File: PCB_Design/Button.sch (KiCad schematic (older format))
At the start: 4 parts, among them SW1 SW_Push

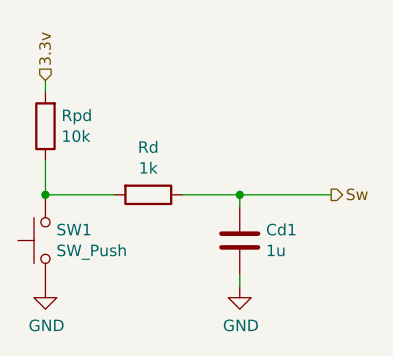
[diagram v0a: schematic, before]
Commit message: huellas agregadas
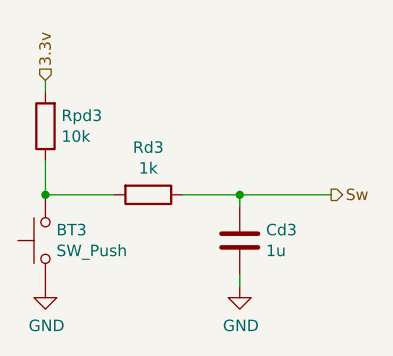
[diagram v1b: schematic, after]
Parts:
- BT1: renamed from SW1; footprint (none) -> Button_Switch_THT:SW_PUSH_6mm_H9.5mm
- Cd1: footprint (none) -> Capacitor_SMD:CP_Elec_3x5.4
- Rd1: renamed from Rd; footprint (none) -> Resistor_SMD:R_0805_2012Metric_Pad1.20x1.40mm_HandSolder
- Rpd1: renamed from Rpd; footprint (none) -> Resistor_SMD:R_0805_2012Metric_Pad1.20x1.40mm_HandSolder
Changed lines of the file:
@@
 $Descr User 5906 5906
 encoding utf-8
-Sheet 6 7
+Sheet 5 7
 Title "Debouncing circuit "
 Date ""
@@
 $EndDescr
 $Comp
-L Switch:SW_Push SW1
+L Switch:SW_Push BT1
 U 1 1 61AF23CF
 P 2550 2650
-AR Path="/61AF1821/61AF23CF" Ref="SW1"  Part="1"
-AR Path="/61B0D93C/61AF23CF" Ref="SW3"  Part="1"
-AR Path="/61B0DE61/61AF23CF" Ref="SW2"  Part="1"
-AR Path="/61B0E45E/61AF23CF" Ref="SW4"  Part="1"
-F 0 "SW1" V 2596 2602 50  0000 R CNN
+AR Path="/61AF1821/61AF23CF" Ref="BT1"  Part="1"
+AR Path="/61B0D93C/61AF23CF" Ref="BT3"  Part="1"
+AR Path="/61B0DE61/61AF23CF" Ref="BT2"  Part="1"
+AR Path="/61B0E45E/61AF23CF" Ref="BT4"  Part="1"
+F 0 "BT3" V 2596 2602 50  0000 R CNN
 F 1 "SW_Push" V 2505 2602 50  0000 R CNN
-F 2 "" H 2550 2850 50  0001 C CNN
+F 2 "Button_Switch_THT:SW_PUSH_6mm_H9.5mm" H 2550 2850 50  0001 C CNN
 F 3 "~" H 2550 2850 50  0001 C CNN
 	1    2550 2650
@@
 $EndComp
 $Comp
-L Device:R Rd
+L Device:R Rd1
 U 1 1 61AF40E8
 P 3000 2450
-AR Path="/61AF1821/61AF40E8" Ref="Rd"  Part="1"
+AR Path="/61AF1821/61AF40E8" Ref="Rd1"  Part="1"
 AR Path="/61B0D93C/61AF40E8" Ref="Rd3"  Part="1"
 AR Path="/61B0DE61/61AF40E8" Ref="Rd2"  Part="1"
 AR Path="/61B0E45E/61AF40E8" Ref="Rd4"  Part="1"
-F 0 "Rd" V 2793 2450 50  0000 C CNN
+F 0 "Rd3" V 2793 2450 50  0000 C CNN
 F 1 "1k" V 2884 2450 50  0000 C CNN
-F 2 "" V 2930 2450 50  0001 C CNN
+F 2 "Resistor_SMD:R_0805_2012Metric_Pad1.20x1.40mm_HandSolder" V 2930 2450 50  0001 C CNN
 F 3 "~" H 3000 2450 50  0001 C CNN
 	1    3000 2450
@@
 AR Path="/61B0DE61/61AF4C44" Ref="Cd2"  Part="1"
 AR Path="/61B0E45E/61AF4C44" Ref="Cd4"  Part="1"
-F 0 "Cd1" H 3285 2604 50  0000 R CNN
+F 0 "Cd3" H 3285 2604 50  0000 R CNN
 F 1 "1u" H 3285 2695 50  0000 R CNN
-F 2 "" H 3438 2500 50  0001 C CNN
+F 2 "Capacitor_SMD:CP_Elec_3x5.4" H 3438 2500 50  0001 C CNN
 F 3 "~" H 3400 2650 50  0001 C CNN
 	1    3400 2650
@@
 $EndComp
 $Comp
-L Device:R Rpd
+L Device:R Rpd1
 U 1 1 61AFF83B
 P 2550 2150
-AR Path="/61AF1821/61AFF83B" Ref="Rpd"  Part="1"
+AR Path="/61AF1821/61AFF83B" Ref="Rpd1"  Part="1"
 AR Path="/61B0D93C/61AFF83B" Ref="Rpd3"  Part="1"
 AR Path="/61B0DE61/61AFF83B" Ref="Rpd2"  Part="1"
 AR Path="/61B0E45E/61AFF83B" Ref="Rpd4"  Part="1"
-F 0 "Rpd" H 2480 2104 50  0000 R CNN
+F 0 "Rpd3" H 2480 2104 50  0000 R CNN
 F 1 "10k" H 2480 2195 50  0000 R CNN
-F 2 "" V 2480 2150 50  0001 C CNN
+F 2 "Resistor_SMD:R_0805_2012Metric_Pad1.20x1.40mm_HandSolder" V 2480 2150 50  0001 C CNN
 F 3 "~" H 2550 2150 50  0001 C CNN
 	1    2550 2150

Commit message: Falta tetris
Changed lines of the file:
@@
 $Descr User 5906 5906
 encoding utf-8
-Sheet 5 7
+Sheet 6 7
 Title "Debouncing circuit "
 Date ""
@@
 AR Path="/61B0DE61/61AF23CF" Ref="BT2"  Part="1"
 AR Path="/61B0E45E/61AF23CF" Ref="BT4"  Part="1"
-F 0 "BT3" V 2596 2602 50  0000 R CNN
+F 0 "BT1" V 2596 2602 50  0000 R CNN
 F 1 "SW_Push" V 2505 2602 50  0000 R CNN
 F 2 "Button_Switch_THT:SW_PUSH_6mm_H9.5mm" H 2550 2850 50  0001 C CNN
@@
 AR Path="/61B0DE61/61AF40E8" Ref="Rd2"  Part="1"
 AR Path="/61B0E45E/61AF40E8" Ref="Rd4"  Part="1"
-F 0 "Rd3" V 2793 2450 50  0000 C CNN
+F 0 "Rd1" V 2793 2450 50  0000 C CNN
 F 1 "1k" V 2884 2450 50  0000 C CNN
 F 2 "Resistor_SMD:R_0805_2012Metric_Pad1.20x1.40mm_HandSolder" V 2930 2450 50  0001 C CNN
@@
 AR Path="/61B0DE61/61AF4C44" Ref="Cd2"  Part="1"
 AR Path="/61B0E45E/61AF4C44" Ref="Cd4"  Part="1"
-F 0 "Cd3" H 3285 2604 50  0000 R CNN
+F 0 "Cd1" H 3285 2604 50  0000 R CNN
 F 1 "1u" H 3285 2695 50  0000 R CNN
 F 2 "Capacitor_SMD:CP_Elec_3x5.4" H 3438 2500 50  0001 C CNN
@@
 AR Path="/61B0DE61/61AFF83B" Ref="Rpd2"  Part="1"
 AR Path="/61B0E45E/61AFF83B" Ref="Rpd4"  Part="1"
-F 0 "Rpd3" H 2480 2104 50  0000 R CNN
+F 0 "Rpd1" H 2480 2104 50  0000 R CNN
 F 1 "10k" H 2480 2195 50  0000 R CNN
 F 2 "Resistor_SMD:R_0805_2012Metric_Pad1.20x1.40mm_HandSolder" V 2480 2150 50  0001 C CNN
@@
 AR Path="/61B0DE61/61B006D1" Ref="#PWR0113"  Part="1"
 AR Path="/61B0E45E/61B006D1" Ref="#PWR0115"  Part="1"
-F 0 "#PWR0119" H 3400 2600 50  0001 C CNN
+F 0 "#PWR0117" H 3400 2600 50  0001 C CNN
 F 1 "GND" H 3405 2677 50  0000 C CNN
 F 2 "" H 3400 2850 50  0001 C CNN
@@
 AR Path="/61B0DE61/61B01C2D" Ref="#PWR0114"  Part="1"
 AR Path="/61B0E45E/61B01C2D" Ref="#PWR0116"  Part="1"
-F 0 "#PWR0120" H 2550 2600 50  0001 C CNN
+F 0 "#PWR0118" H 2550 2600 50  0001 C CNN
 F 1 "GND" H 2555 2677 50  0000 C CNN
 F 2 "" H 2550 2850 50  0001 C CNN

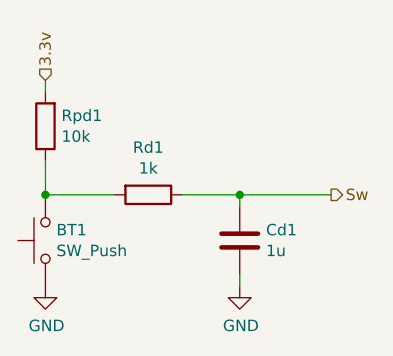
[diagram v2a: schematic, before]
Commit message: Nuevas huellas y un poco más de orden
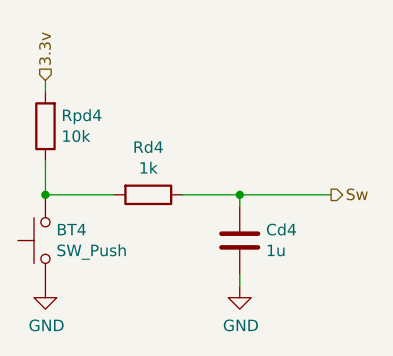
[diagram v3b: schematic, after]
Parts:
- Cd1: footprint Capacitor_SMD:CP_Elec_3x5.4 -> Capacitor_SMD:C_0805_2012Metric_Pad1.18x1.45mm_HandSolder
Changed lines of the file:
@@
 $Descr User 5906 5906
 encoding utf-8
-Sheet 6 7
+Sheet 5 7
 Title "Debouncing circuit "
 Date ""
@@
 AR Path="/61B0DE61/61AF23CF" Ref="BT2"  Part="1"
 AR Path="/61B0E45E/61AF23CF" Ref="BT4"  Part="1"
-F 0 "BT1" V 2596 2602 50  0000 R CNN
+F 0 "BT4" V 2596 2602 50  0000 R CNN
 F 1 "SW_Push" V 2505 2602 50  0000 R CNN
 F 2 "Button_Switch_THT:SW_PUSH_6mm_H9.5mm" H 2550 2850 50  0001 C CNN
@@
 AR Path="/61B0DE61/61AF40E8" Ref="Rd2"  Part="1"
 AR Path="/61B0E45E/61AF40E8" Ref="Rd4"  Part="1"
-F 0 "Rd1" V 2793 2450 50  0000 C CNN
+F 0 "Rd4" V 2793 2450 50  0000 C CNN
 F 1 "1k" V 2884 2450 50  0000 C CNN
 F 2 "Resistor_SMD:R_0805_2012Metric_Pad1.20x1.40mm_HandSolder" V 2930 2450 50  0001 C CNN
@@
 AR Path="/61B0DE61/61AF4C44" Ref="Cd2"  Part="1"
 AR Path="/61B0E45E/61AF4C44" Ref="Cd4"  Part="1"
-F 0 "Cd1" H 3285 2604 50  0000 R CNN
+F 0 "Cd4" H 3285 2604 50  0000 R CNN
 F 1 "1u" H 3285 2695 50  0000 R CNN
-F 2 "Capacitor_SMD:CP_Elec_3x5.4" H 3438 2500 50  0001 C CNN
+F 2 "Capacitor_SMD:C_0805_2012Metric_Pad1.18x1.45mm_HandSolder" H 3438 2500 50  0001 C CNN
 F 3 "~" H 3400 2650 50  0001 C CNN
 	1    3400 2650
@@
 AR Path="/61B0DE61/61AFF83B" Ref="Rpd2"  Part="1"
 AR Path="/61B0E45E/61AFF83B" Ref="Rpd4"  Part="1"
-F 0 "Rpd1" H 2480 2104 50  0000 R CNN
+F 0 "Rpd4" H 2480 2104 50  0000 R CNN
 F 1 "10k" H 2480 2195 50  0000 R CNN
 F 2 "Resistor_SMD:R_0805_2012Metric_Pad1.20x1.40mm_HandSolder" V 2480 2150 50  0001 C CNN
@@
 AR Path="/61B0DE61/61B006D1" Ref="#PWR0113"  Part="1"
 AR Path="/61B0E45E/61B006D1" Ref="#PWR0115"  Part="1"
-F 0 "#PWR0117" H 3400 2600 50  0001 C CNN
+F 0 "#PWR0119" H 3400 2600 50  0001 C CNN
 F 1 "GND" H 3405 2677 50  0000 C CNN
 F 2 "" H 3400 2850 50  0001 C CNN
@@
 AR Path="/61B0DE61/61B01C2D" Ref="#PWR0114"  Part="1"
 AR Path="/61B0E45E/61B01C2D" Ref="#PWR0116"  Part="1"
-F 0 "#PWR0118" H 2550 2600 50  0001 C CNN
+F 0 "#PWR0120" H 2550 2600 50  0001 C CNN
 F 1 "GND" H 2555 2677 50  0000 C CNN
 F 2 "" H 2550 2850 50  0001 C CNN

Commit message: PCB organizada con casi todo SMD
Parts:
- BT1: footprint Button_Switch_THT:SW_PUSH_6mm_H9.5mm -> Button_Switch_SMD:SW_Push_1P1T_NO_6x6mm_H9.5mm
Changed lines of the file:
@@
 F 0 "BT4" V 2596 2602 50  0000 R CNN
 F 1 "SW_Push" V 2505 2602 50  0000 R CNN
-F 2 "Button_Switch_THT:SW_PUSH_6mm_H9.5mm" H 2550 2850 50  0001 C CNN
+F 2 "Button_Switch_SMD:SW_Push_1P1T_NO_6x6mm_H9.5mm" H 2550 2850 50  0001 C CNN
 F 3 "~" H 2550 2850 50  0001 C CNN
 	1    2550 2650

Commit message: PCB diseño fianl retocado + lista componentes
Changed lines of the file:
@@
 $Descr User 5906 5906
 encoding utf-8
-Sheet 5 7
+Sheet 6 7
 Title "Debouncing circuit "
 Date ""
@@
 AR Path="/61B0DE61/61AF23CF" Ref="BT2"  Part="1"
 AR Path="/61B0E45E/61AF23CF" Ref="BT4"  Part="1"
-F 0 "BT4" V 2596 2602 50  0000 R CNN
+F 0 "BT3" V 2596 2602 50  0000 R CNN
 F 1 "SW_Push" V 2505 2602 50  0000 R CNN
 F 2 "Button_Switch_SMD:SW_Push_1P1T_NO_6x6mm_H9.5mm" H 2550 2850 50  0001 C CNN
@@
 AR Path="/61B0DE61/61AF40E8" Ref="Rd2"  Part="1"
 AR Path="/61B0E45E/61AF40E8" Ref="Rd4"  Part="1"
-F 0 "Rd4" V 2793 2450 50  0000 C CNN
+F 0 "Rd3" V 2793 2450 50  0000 C CNN
 F 1 "1k" V 2884 2450 50  0000 C CNN
 F 2 "Resistor_SMD:R_0805_2012Metric_Pad1.20x1.40mm_HandSolder" V 2930 2450 50  0001 C CNN
@@
 AR Path="/61B0DE61/61AF4C44" Ref="Cd2"  Part="1"
 AR Path="/61B0E45E/61AF4C44" Ref="Cd4"  Part="1"
-F 0 "Cd4" H 3285 2604 50  0000 R CNN
+F 0 "Cd3" H 3285 2604 50  0000 R CNN
 F 1 "1u" H 3285 2695 50  0000 R CNN
 F 2 "Capacitor_SMD:C_0805_2012Metric_Pad1.18x1.45mm_HandSolder" H 3438 2500 50  0001 C CNN
@@
 AR Path="/61B0DE61/61AFF83B" Ref="Rpd2"  Part="1"
 AR Path="/61B0E45E/61AFF83B" Ref="Rpd4"  Part="1"
-F 0 "Rpd4" H 2480 2104 50  0000 R CNN
+F 0 "Rpd3" H 2480 2104 50  0000 R CNN
 F 1 "10k" H 2480 2195 50  0000 R CNN
 F 2 "Resistor_SMD:R_0805_2012Metric_Pad1.20x1.40mm_HandSolder" V 2480 2150 50  0001 C CNN

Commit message: PCB terminada
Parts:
- Cd1: value 1u -> 0.1u
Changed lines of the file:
@@
 $Descr User 5906 5906
 encoding utf-8
-Sheet 6 7
+Sheet 5 7
 Title "Debouncing circuit "
 Date ""
@@
 AR Path="/61B0DE61/61AF23CF" Ref="BT2"  Part="1"
 AR Path="/61B0E45E/61AF23CF" Ref="BT4"  Part="1"
-F 0 "BT3" V 2596 2602 50  0000 R CNN
+F 0 "BT4" V 2596 2602 50  0000 R CNN
 F 1 "SW_Push" V 2505 2602 50  0000 R CNN
 F 2 "Button_Switch_SMD:SW_Push_1P1T_NO_6x6mm_H9.5mm" H 2550 2850 50  0001 C CNN
@@
 AR Path="/61B0DE61/61AF40E8" Ref="Rd2"  Part="1"
 AR Path="/61B0E45E/61AF40E8" Ref="Rd4"  Part="1"
-F 0 "Rd3" V 2793 2450 50  0000 C CNN
+F 0 "Rd4" V 2793 2450 50  0000 C CNN
 F 1 "1k" V 2884 2450 50  0000 C CNN
 F 2 "Resistor_SMD:R_0805_2012Metric_Pad1.20x1.40mm_HandSolder" V 2930 2450 50  0001 C CNN
@@
 AR Path="/61B0DE61/61AF4C44" Ref="Cd2"  Part="1"
 AR Path="/61B0E45E/61AF4C44" Ref="Cd4"  Part="1"
-F 0 "Cd3" H 3285 2604 50  0000 R CNN
-F 1 "1u" H 3285 2695 50  0000 R CNN
+F 0 "Cd4" H 3285 2604 50  0000 R CNN
+F 1 "0.1u" H 3285 2695 50  0000 R CNN
 F 2 "Capacitor_SMD:C_0805_2012Metric_Pad1.18x1.45mm_HandSolder" H 3438 2500 50  0001 C CNN
 F 3 "~" H 3400 2650 50  0001 C CNN
@@
 AR Path="/61B0DE61/61AFF83B" Ref="Rpd2"  Part="1"
 AR Path="/61B0E45E/61AFF83B" Ref="Rpd4"  Part="1"
-F 0 "Rpd3" H 2480 2104 50  0000 R CNN
+F 0 "Rpd4" H 2480 2104 50  0000 R CNN
 F 1 "10k" H 2480 2195 50  0000 R CNN
 F 2 "Resistor_SMD:R_0805_2012Metric_Pad1.20x1.40mm_HandSolder" V 2480 2150 50  0001 C CNN
